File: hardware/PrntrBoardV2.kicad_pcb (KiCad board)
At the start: 2 copper layers, 148.7 x 104.3 mm, 248 parts, among them J10 Conn_01x03_Male, J11 Conn_01x03_Male, J12 Conn_01x03_Male, J13 Conn_01x03_Male, J14 Conn_01x03_Male, J15 Conn_01x03_Male, J16 JST XH, J17 KF350, J18 JST XH, J19 JST XH, J20 KF350, J21 JST XH, J3 USB_B_Micro, J4 JST XH, J5 KF129, J6 KF350, J7 Conn_01x03_Male, J8 Conn_01x03_Male, J9 Conn_01x03_Male, U1 74LVC125, U2 STM32F407VETx, U3 24LC64, U4 AMS1117-3.3, U5 DCBuck, U6 74HCT02, Y1 8MHz

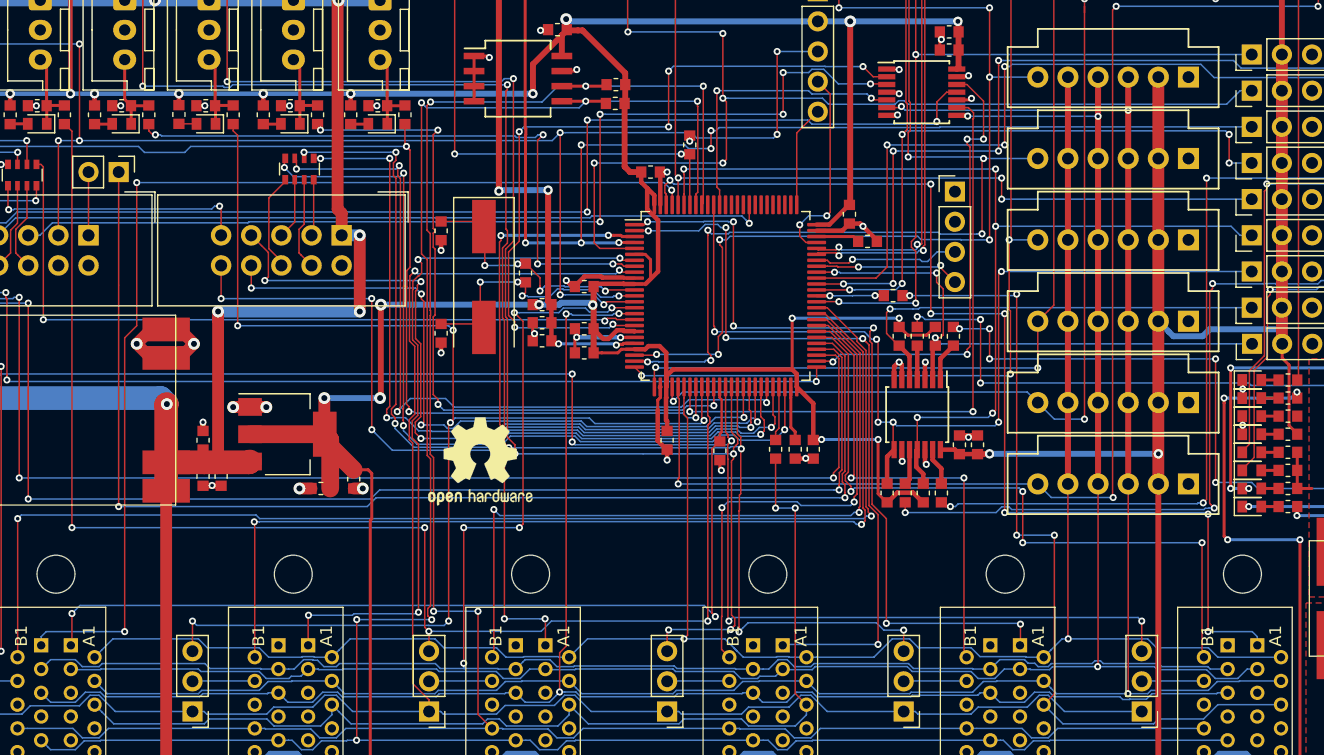
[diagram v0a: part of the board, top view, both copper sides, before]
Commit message: 10 untrouted tracks.
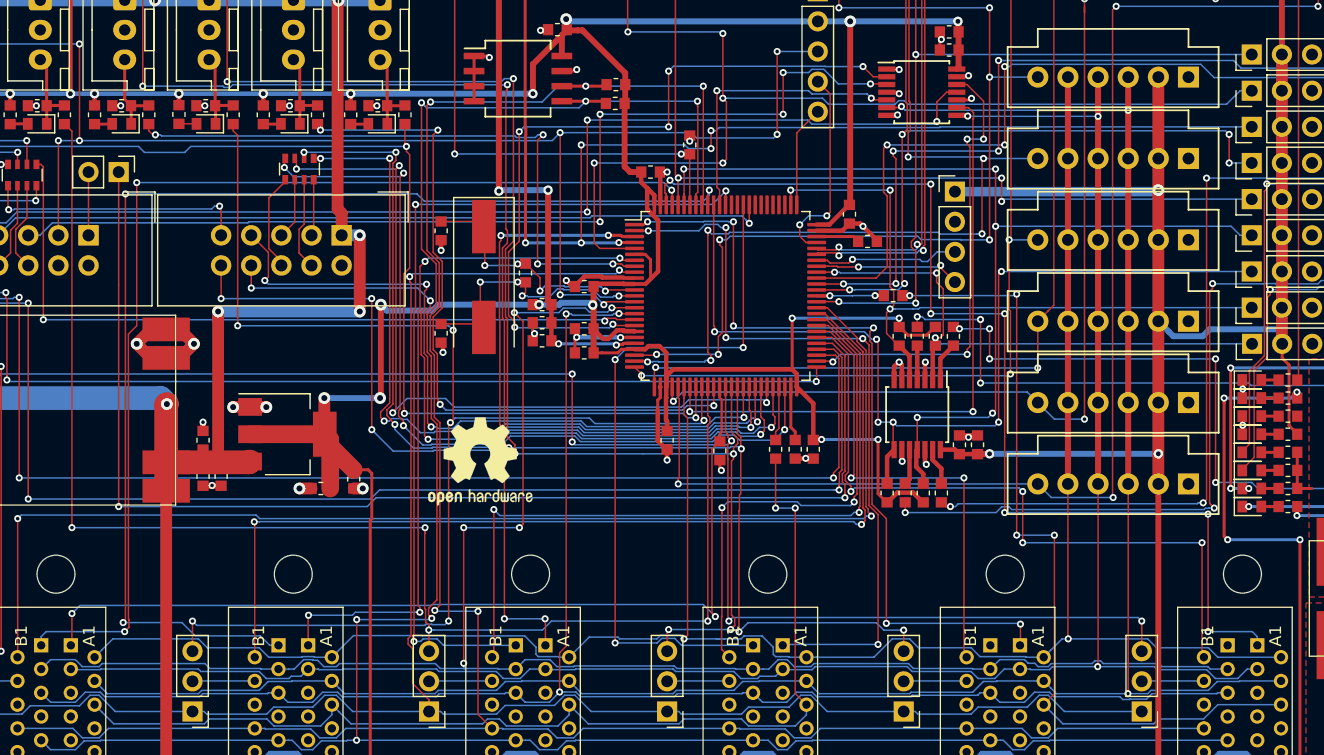
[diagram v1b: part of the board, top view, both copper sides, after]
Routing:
- net ST2_STEP: track 0.00 -> 101.5 mm, vias 0 -> 3
- net ST3_STEP: track 0.00 -> 73.6 mm, vias 0 -> 3
- net ST4_STEP: track 0.00 -> 59.2 mm, vias 0 -> 3
- net PWM2: track 37.4 -> 57.3 mm, vias 1 -> 3
- net 5V: track 426.6 -> 443.8 mm, vias 13 -> 14
- net SPI1_MISO: track 175.7 -> 177.5 mm
- net ~ST2_CS: track 61.1 -> 59.7 mm
- net LCD_D7: track 64.1 -> 65.1 mm
- net I2C_SDA: track 200.2 -> 201.1 mm
- net I2C_SCL: track 198.1 -> 199.0 mm

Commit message: All routed!!!
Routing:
- net 3.3V: track 516.6 -> 608.7 mm, vias 26 -> 30
- net SDIO_CLK: track 3.90 -> 86.3 mm, vias 2 -> 4
- net ~SD_DETECT: track 65.8 -> 147.7 mm, vias 1 -> 5
- net SDIO_CMD: track 2.72 -> 84.5 mm, vias 0 -> 2
- net SDIO_D2: track 2.67 -> 80.5 mm, vias 0 -> 2
- net SDIO_D3: track 2.60 -> 79.7 mm, vias 0 -> 2
- net ST6_STEP: track 0.00 -> 76.1 mm, vias 0 -> 5
- net ST5_STEP: track 0.00 -> 61.7 mm, vias 0 -> 4
- net AVREF: track 146.1 -> 148.0 mm
- net ADC1: track 91.4 -> 92.5 mm
- net PWM4: track 84.3 -> 85.2 mm
- net Net-(R52-Pad1): track 50.0 -> 49.5 mm
- net GND: vias 102 -> 371
- added copper zone on F.Cu, net GND

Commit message: Verification rev 1.
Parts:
- added EXP3: IDC 2x5, Connector_IDC:IDC-Header_2x05_P2.54mm_Vertical, F.Cu at (96.5, 75.6)
- added J1: Fan, Connector_JST:JST_XH_B2B-XH-A_1x02_P2.50mm_Vertical, F.Cu at (71.1, 160.4)
- added J2: Fan, Connector_JST:JST_XH_B2B-XH-A_1x02_P2.50mm_Vertical, F.Cu at (131.2, 160.4)
- added J22: Fan, Connector_JST:JST_XH_B2B-XH-A_1x02_P2.50mm_Vertical, F.Cu at (51.6, 160.5)
- added J23: Fan, Connector_JST:JST_XH_B2B-XH-A_1x02_P2.50mm_Vertical, F.Cu at (151.3, 160.5)
- moved LOGO1 9.40 mm to (86.5, 119.6)
- moved C11 3.39 mm to (86.9, 82.9), turned to 0 degrees
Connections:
- U2 pad 86: (no net) -> UART2_TX
- U2 pad 87: (no net) -> UART2_RX
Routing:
- net ~EXP_CS: track 104.7 -> 173.9 mm, vias 2 -> 6
- net 5V: track 444.0 -> 513.0 mm, vias 14 -> 17
- net UART_TX: track 12.4 -> 61.1 mm, vias 2 -> 3
- net UART_RX: track 12.3 -> 60.0 mm, vias 1 -> 2
- net UART2_TX: track 0.00 -> 36.9 mm, vias 0 -> 1
- net UART2_RX: track 0.00 -> 32.3 mm, vias 0 -> 1
- net I2C_SDA: track 201.1 -> 211.3 mm
- net I2C_SCL: track 199.0 -> 207.5 mm
- net GND: track 172.0 -> 171.3 mm, vias 371 -> 419
- net PWM5: track 110.4 -> 111.0 mm
- net 3.3V: track 608.7 -> 608.6 mm, vias 30 -> 32
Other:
- outline, holes or cut-outs redrawn
- board text added: "(c) iQury.us Oct 2019"
- board text added: "12-24V"
- board text added: "12-24V (- +)"
- board text added: "12-24V + -"
- board text added: "3.3V"
- board text added: "3x10A"
- board text added: "5V"
- board text added: "5V + -"
- board text added: "BED"
- board text added: "BEEP"
- board text added: "BOOT"
- board text added: "BTN_ENC"
- board text added: "ENC_A"
- board text added: "ENC_B"
- board text added: "EXP1"
- board text added: "EXP2"
- board text added: "EXP3"
- board text added: "Endstops"
- board text added: "F1"
- board text added: "F2"
- board text added: "F3"
- board text added: "F4"
- board text added: "F5"
- board text added: "Fan"
- board text added: "Fan 1 - +"
- board text added: "Fan 2 - +"
- board text added: "Fan 3 - +"
- board text added: "Fan 4 - +"
- board text added: "Fan 5 - +"
- board text added: "Fan voltage"
- board text added: "G | U-"
- board text added: "G | V-"
- board text added: "G | X-"
- board text added: "G | Y-"
- board text added: "G | Z+"
- board text added: "G | Z-"
- board text added: "GND"
- board text added: "H1"
- board text added: "H2"
- board text added: "H3"
- board text added: "H4"
- board text added: "HTR1"
- board text added: "HTR2"
- board text added: "HTR3"
- board text added: "Heater 1 (bed) - +"
- board text added: "Heater 2 - +"
- board text added: "Heater 3 - +"
- board text added: "Heater 4 - +"
- board text added: "KILL"
- board text added: "LCD_D4"
- board text added: "LCD_D5"
- board text added: "LCD_D6"
- board text added: "LCD_D7"
- board text added: "LCD_RS"
- board text added: "MISO"
- board text added: "MOSI"
- board text added: "Mot"
- board text added: "PWM"
- board text added: "PrntrBoard V2"
- board text added: "RESET"
- board text added: "RX"
- board text added: "RX1"
- board text added: "RX2"
- board text added: "SCK"
- board text added: "SCL"
- board text added: "SDA"
- board text added: "SDWIO"
- board text added: "ST1"
- board text added: "ST2"
- board text added: "ST3"
- board text added: "ST4"
- board text added: "ST5"
- board text added: "ST6"
- board text added: "SWDCLK"
- board text added: "Sensor"
- board text added: "Sensor GND"
- board text added: "Srvo"
- board text added: "TC1"
- board text added: "TC2"
- board text added: "TC3"
- board text added: "TC4"
- board text added: "TC5"
- board text added: "TC6"
- board text added: "TH1"
- board text added: "TH2"
- board text added: "TH3"
- board text added: "TH4"
- board text added: "TH5"
- board text added: "TH6"
- board text added: "TX"
- board text added: "TX1"
- board text added: "TX2"
- board text added: "Thermistors"
- board text added: "Thermocouples"
- board text added: "U-"
- board text added: "V-"
- board text added: "Vin|5V"
- board text added: "X+"
- board text added: "X-"
- board text added: "Y+"
- board text added: "Y-"
- board text added: "Z+"
- board text added: "Z-"
- board text added: "https://blog.pcbxptr.com"
- board text added: "rev 1"
- board text added: "swd"
- board text added: "~CS"
- board text added: "~LCD_E"
- board text added: "~RESET"
- board text added: "~SD_CS"

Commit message: Start rev 2.
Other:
- board text added: "rev 2"
- board text removed: "rev 1"

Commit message: What is more embarasin than a typo on the silk screen?
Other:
- board text added: "https://blog.pcbxprt.com"
- board text removed: "https://blog.pcbxptr.com"

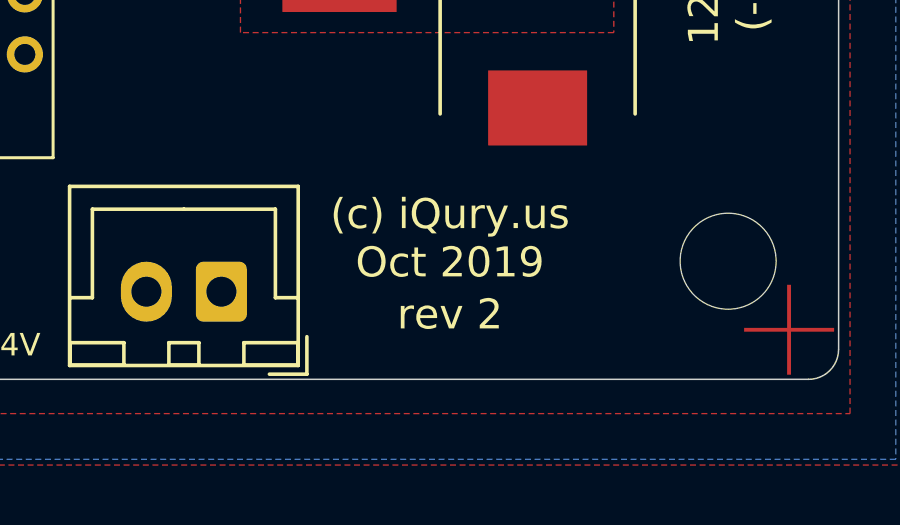
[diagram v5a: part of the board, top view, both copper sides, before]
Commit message: Update the gerber files with the fixed typo.
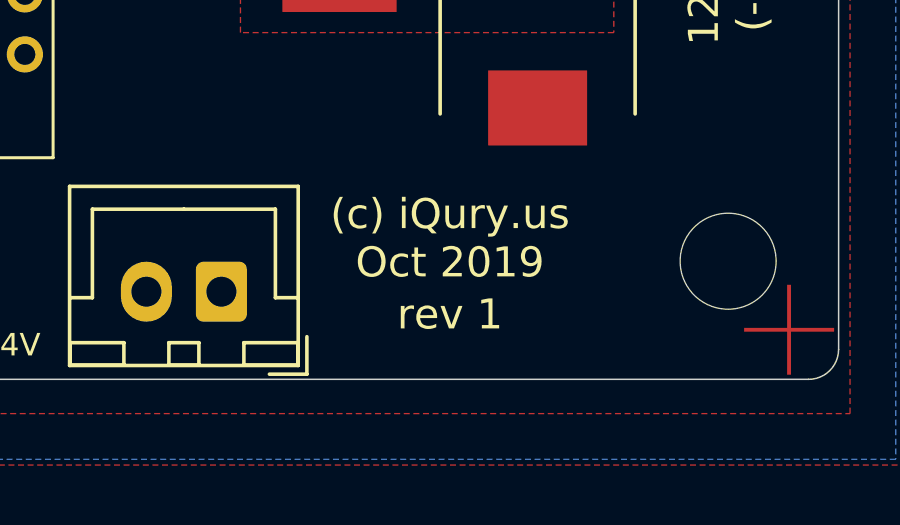
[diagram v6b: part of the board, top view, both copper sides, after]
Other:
- board text added: "rev 1"
- board text removed: "rev 2"
